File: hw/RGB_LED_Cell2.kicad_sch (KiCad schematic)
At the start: 4 parts

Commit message: updated Designs
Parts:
- added Q15: 2N7002T, IotPi_Package_TO_SOT_SMD:SOT-523_no-silkscreen, symbol Device:Q_NMOS_GSD
- D2: footprint IotPi_LED:XL-1615RGBC -> IotPi_LED:XL-1615RGBC_no-silkscreen
- R7, R8, R9: footprint Resistor_SMD:R_0402_1005Metric_Pad0.72x0.64mm_HandSolder -> Resistor_SMD:R_0402_1005Metric
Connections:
- net HighSide_Input: now also Q15.1 (G); no longer D2.3 (A)
- new net: D2.3 (A), Q15.2 (S)
- new net VDD: Q15.3 (D)

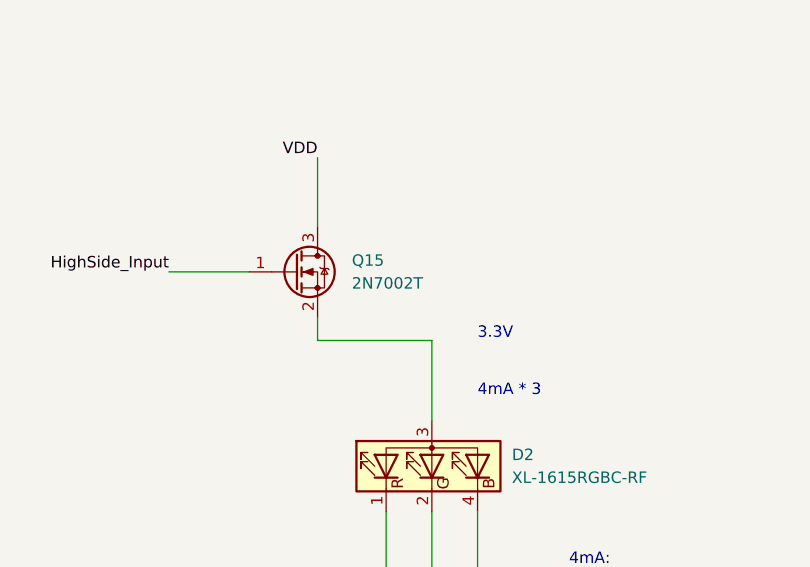
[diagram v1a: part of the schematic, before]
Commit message: replace all N-MOS components
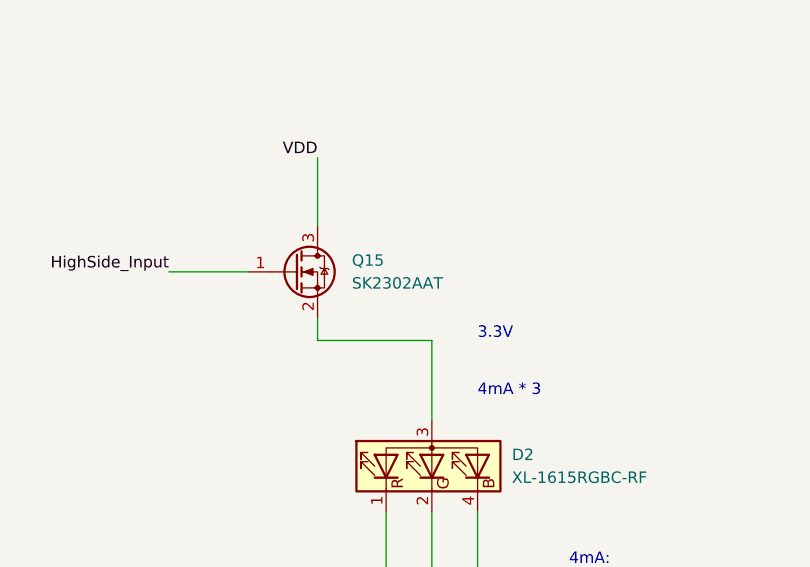
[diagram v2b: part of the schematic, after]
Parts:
- Q15: value 2N7002T -> SK2302AAT; LCSC C5224243 -> C475757; Vendor ElecSuper(静芯微） -> SHIKUES(时科); Vendor Model 2N7002T -> SK2302AAT
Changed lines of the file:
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@@
       (effects (font (size 1.27 1.27)) (justify left))
     )
-    (property "Value" "2N7002T" (at 138.43 66.04 0)
+    (property "Value" "SK2302AAT" (at 138.43 66.04 0)
       (effects (font (size 1.27 1.27)) (justify left))
     )
@@
       (effects (font (size 1.27 1.27)) hide)
     )
-    (property "Description" "类型: N沟道 漏源电压(Vdss): 60V 连续漏极电流(Id): 300mA 功率(Pd): 200mW 导通电阻(RDS(on)@Vgs,Id):" (at 132.08 64.77 0)
+    (property "Description" "类型：N沟道 漏源电压(Vdss)：20V 连续漏极电流(Id)：2.1A 功率(Pd)：350mW 导通电阻(RDS(on)@Vgs,Id)：60mΩ@4.5V,2A" (at 132.08 64.77 0)
       (effects (font (size 1.27 1.27)) hide)
     )
-    (property "LCSC" "C5224243" (at 132.08 64.77 0)
+    (property "LCSC" "C475757" (at 132.08 64.77 0)
       (effects (font (size 1.27 1.27)) hide)
     )
-    (property "Vendor" "ElecSuper(静芯微）" (at 132.08 64.77 0)
+    (property "Vendor" " SHIKUES(时科)" (at 132.08 64.77 0)
       (effects (font (size 1.27 1.27)) hide)
     )
-    (property "Vendor Model" "2N7002T" (at 132.08 64.77 0)
+    (property "Vendor Model" "SK2302AAT" (at 132.08 64.77 0)
       (effects (font (size 1.27 1.27)) hide)
     )
